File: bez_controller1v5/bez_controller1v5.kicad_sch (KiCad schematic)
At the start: 66 parts, among them J1 Conn_01x03_Male, J10 Screw_Terminal_01x02, J11 Conn_01x03_Male, J12 USB_B_Mini, J2 Conn_01x03_Male, J3 Conn_01x03_Male, J4 Conn_01x03_Male, J5 Conn_01x03_Male, J6 Conn_01x03_Male, J7 Conn_01x03_Male, J8 IMU Conn_01x08_Female, J9 JTAG Conn_01x06_Male, U1 74LVC2G241, U10 USBLC6-4SC6, U11 STM32F446RETx, U2 74LVC2G241, U3 74LVC2G241, U4 74LVC2G241, U5 74LVC2G241, U6 74LVC2G241, U7 PX07806-500-S, U8 LF50ABV_TO220, U9 LD1117AS33TR_SOT223, Y1 8MHz

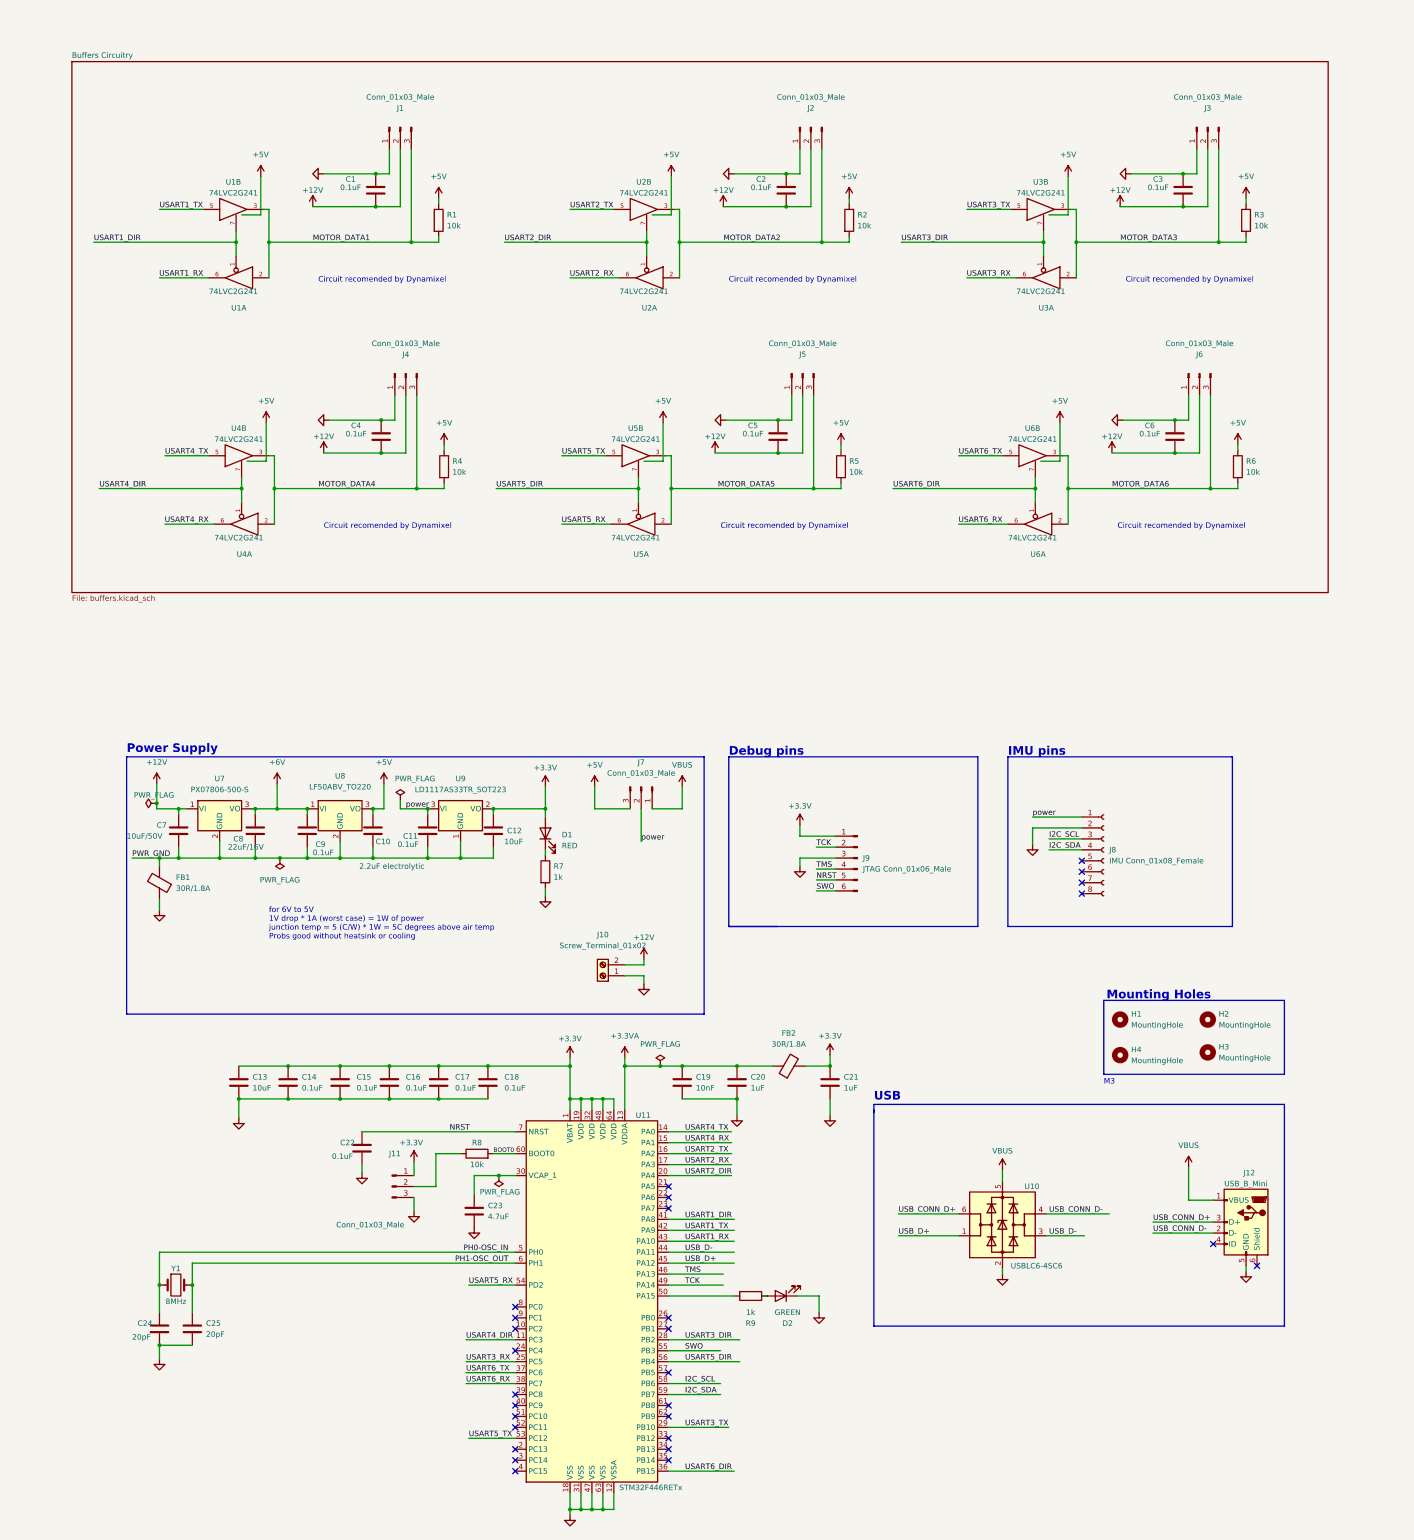
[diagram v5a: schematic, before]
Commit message: Added a means of measuring battery voltage and current + circuit protection
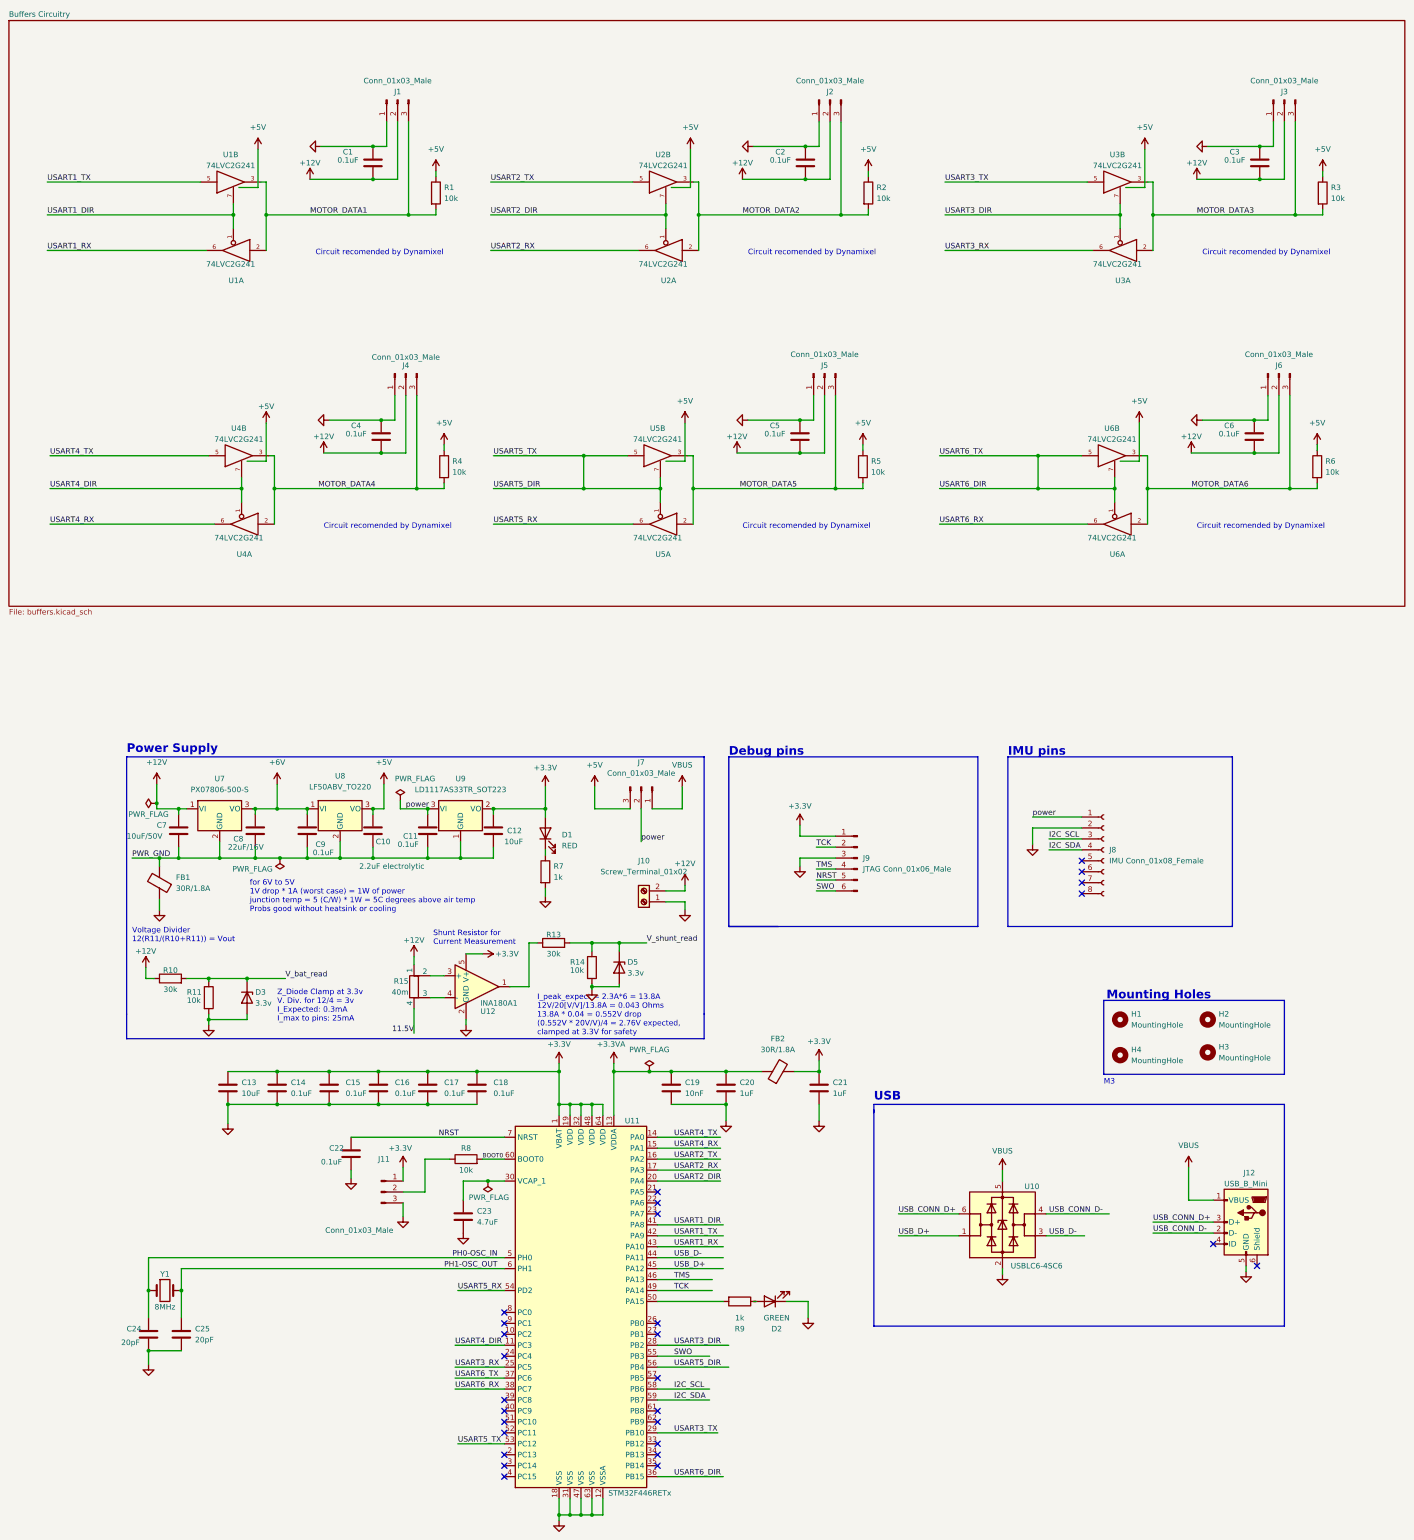
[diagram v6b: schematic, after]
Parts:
- added D3, D5: 3.3v, symbol Device:D_Zener
- added R10, R13: 30k, symbol Device:R
- added R11, R14: 10k, symbol Device:R
- added R15: 40m, symbol Device:R_Shunt
- added U12: INA180A1, Package_TO_SOT_SMD:SOT-23-5, symbol Amplifier_Current:INA180A1
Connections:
- net USART5_TX is gone; now on net USART5_DIR: U11.53 (PC12), U5.5
- net USART6_TX is gone; now on net USART6_DIR: U11.37 (PC6), U6.5
- net +12V: now also R10.1, R15.1
- net +3.3V: now also U12.5 (V+)
- net GND: now also D3.2 (A), D5.2 (A), R11.2, R14.2, U12.2 (GND)
- new net: R13.1, U12.1
- new net: R15.2, U12.3 (+)
- new net: R15.3, U12.4 (-)
- new net 11.5V: R15.4
- new net V_bat_read: D3.1 (K), R10.2, R11.1
- new net V_shunt_read: D5.1 (K), R13.2, R14.1
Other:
- note added: "I_peak_expect = 2.3A*6 = 13.8A 12V/20[V/V]/13.8A = 0.043 Ohms 13.8A * 0.04 = 0.552V drop (0.552V * 20V/V)/4 = 2.76V expected, clamped at 3.3V for safety"
- note added: "Shunt Resistor for Current Measurement"
- note added: "Voltage Divider 12(R11/(R10+R11)) = Vout"
- note added: "Z_Diode Clamp at 3.3v V. Div. for 12/4 = 3v I_Expected: 0.3mA I_max to pins: 25mA"
- moved on the sheet: C1, C13, C14, C15, C16, C17, C18, C19, C2, C20, C21, C22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

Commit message: new rounted PCB
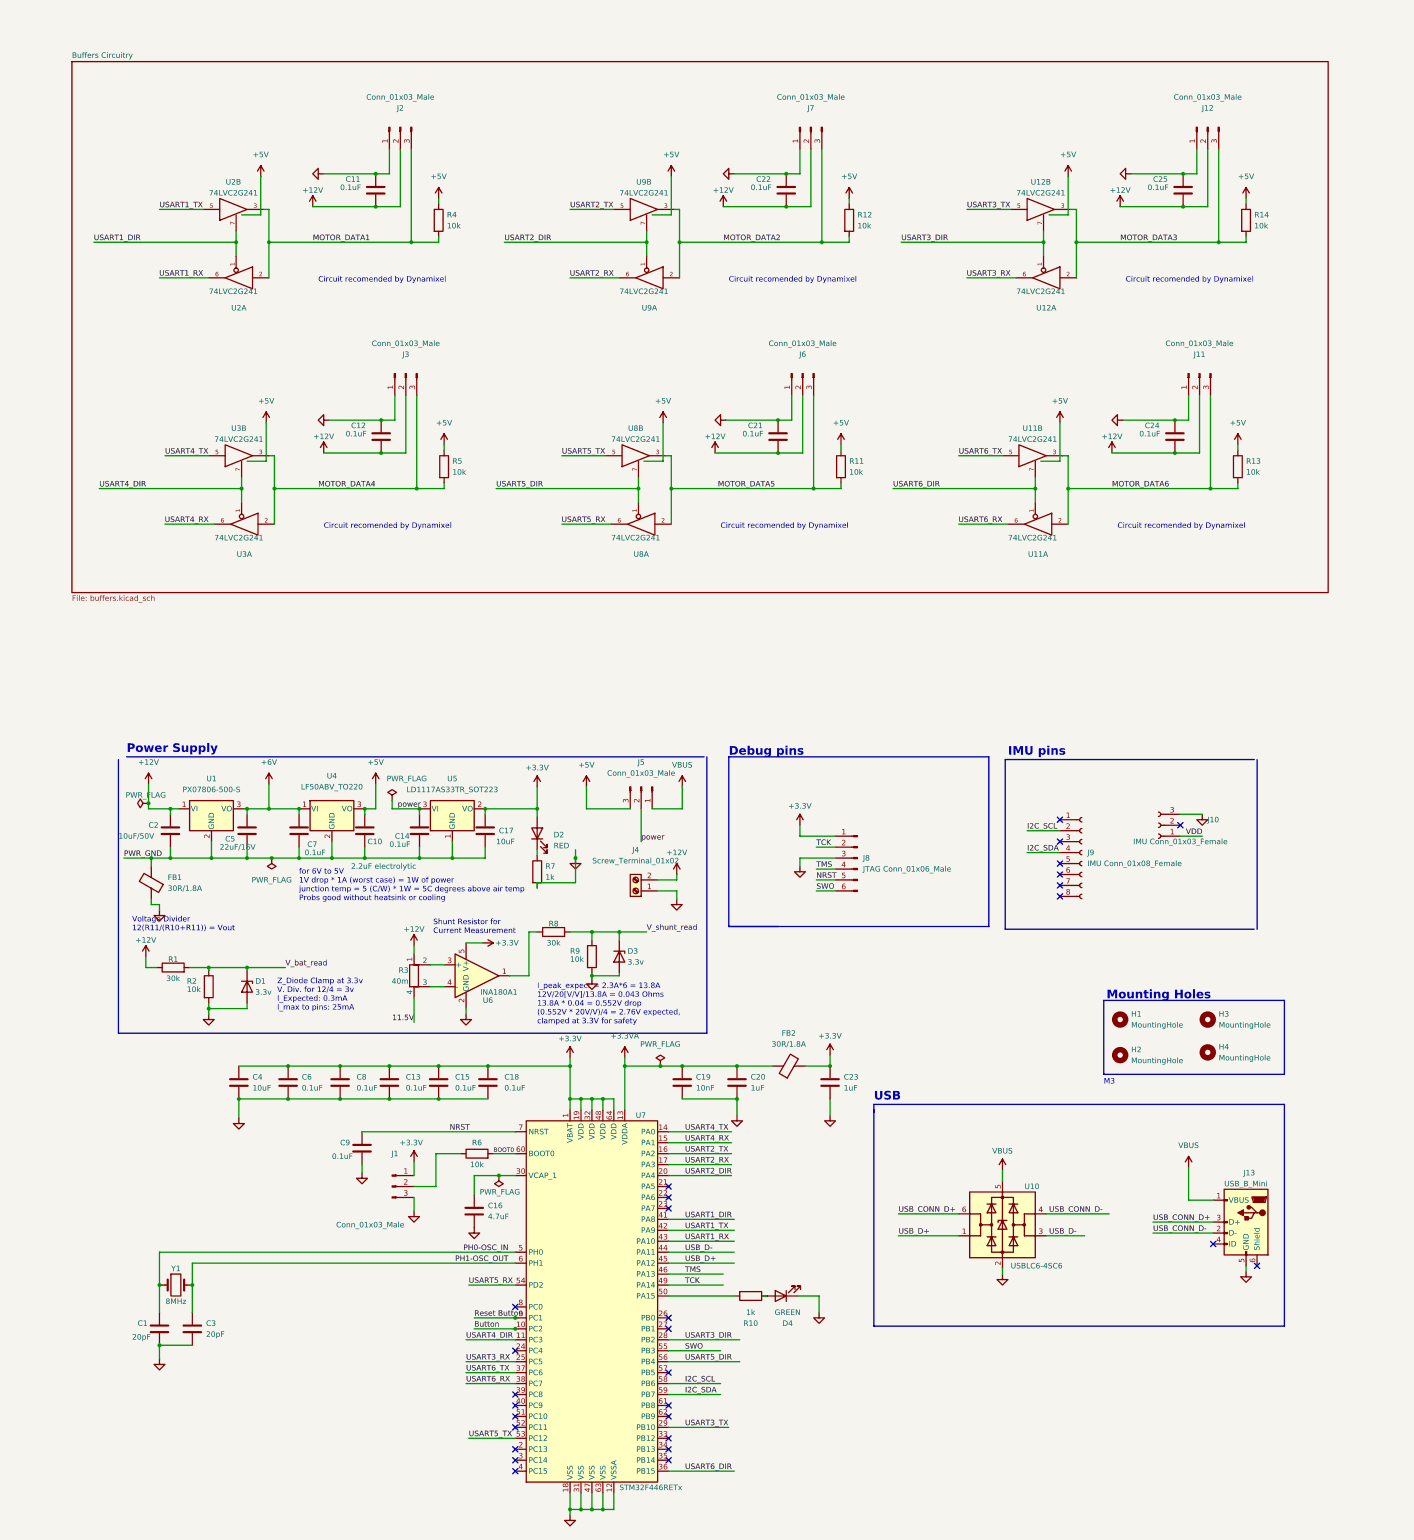
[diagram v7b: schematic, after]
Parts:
- removed D5: 3.3v, symbol Device:D_Zener
- removed R10, R13: 30k, symbol Device:R
- removed R11, R14: 10k, symbol Device:R
- removed R15: 40m, symbol Device:R_Shunt
- removed U12: INA180A1, Package_TO_SOT_SMD:SOT-23-5, symbol Amplifier_Current:INA180A1
- added D1: 3.3v, Diode_SMD:D_0603_1608Metric, symbol Device:D_Zener
- added J10: IMU Conn_01x03_Female, Connector_PinSocket_1.27mm:PinSocket_1x03_P1.27mm_Vertical, symbol Connector:Conn_01x08_Female
- added R1, R8: 30k, Resistor_SMD:R_0603_1608Metric, symbol Device:R
- added R2, R9: 10k, Resistor_SMD:R_0603_1608Metric, symbol Device:R
- added R3: 40m, Resistor_SMD:R_0603_1608Metric, symbol Device:R_Shunt
- added U6: INA180A1, Package_TO_SOT_SMD:SOT-23-5, symbol Amplifier_Current:INA180A1
- C1: renamed from C24; footprint Capacitor_THT:C_Disc_D5.0mm_W2.5mm_P5.00mm -> Capacitor_SMD:C_0603_1608Metric
- C10: footprint Capacitor_THT:C_Radial_D4.0mm_H7.0mm_P1.50mm -> Capacitor_SMD:CP_Elec_4x5.4
- C11: renamed from C1; footprint Capacitor_THT:C_Disc_D5.0mm_W2.5mm_P5.00mm -> Capacitor_SMD:C_0603_1608Metric
- C12: renamed from C4; footprint Capacitor_THT:C_Disc_D5.0mm_W2.5mm_P5.00mm -> Capacitor_SMD:C_0603_1608Metric
- C13: renamed from C16; footprint Capacitor_THT:C_Disc_D5.0mm_W2.5mm_P5.00mm -> Capacitor_SMD:C_0603_1608Metric
- C14: renamed from C11; footprint Capacitor_THT:C_Disc_D5.0mm_W2.5mm_P5.00mm -> Capacitor_SMD:C_0603_1608Metric
- C15: renamed from C17; footprint Capacitor_THT:C_Disc_D5.0mm_W2.5mm_P5.00mm -> Capacitor_SMD:C_0603_1608Metric
- C16: renamed from C23; footprint Capacitor_THT:C_Disc_D5.0mm_W2.5mm_P5.00mm -> Capacitor_SMD:C_0603_1608Metric
- C17: renamed from C12; footprint Capacitor_THT:C_Radial_D5.0mm_H11.0mm_P2.00mm -> Capacitor_SMD:C_0603_1608Metric
- C18, C19, C20: footprint Capacitor_THT:C_Disc_D5.0mm_W2.5mm_P5.00mm -> Capacitor_SMD:C_0603_1608Metric
- C2: renamed from C7; footprint Capacitor_THT:C_Radial_D5.0mm_H11.0mm_P2.00mm -> Capacitor_SMD:C_0805_2012Metric
- C21: renamed from C5; footprint Capacitor_THT:C_Disc_D5.0mm_W2.5mm_P5.00mm -> Capacitor_SMD:C_0603_1608Metric
- C22: renamed from C2; footprint Capacitor_THT:C_Disc_D5.0mm_W2.5mm_P5.00mm -> Capacitor_SMD:C_0603_1608Metric
- C23: renamed from C21; footprint Capacitor_THT:C_Disc_D5.0mm_W2.5mm_P5.00mm -> Capacitor_SMD:C_0603_1608Metric
- C24: renamed from C6; footprint Capacitor_THT:C_Disc_D5.0mm_W2.5mm_P5.00mm -> Capacitor_SMD:C_0603_1608Metric
- C25: renamed from C3; footprint Capacitor_THT:C_Disc_D5.0mm_W2.5mm_P5.00mm -> Capacitor_SMD:C_0603_1608Metric
- C3: renamed from C25; footprint Capacitor_THT:C_Disc_D5.0mm_W2.5mm_P5.00mm -> Capacitor_SMD:C_0603_1608Metric
- C4: renamed from C13; footprint Capacitor_THT:C_Radial_D5.0mm_H11.0mm_P2.00mm -> Capacitor_SMD:C_0603_1608Metric
- C5: renamed from C8; footprint Capacitor_THT:C_Radial_D5.0mm_H11.0mm_P2.00mm -> Capacitor_SMD:C_0805_2012Metric
- C6: renamed from C14; footprint Capacitor_THT:C_Disc_D5.0mm_W2.5mm_P5.00mm -> Capacitor_SMD:C_0603_1608Metric
- C7: renamed from C9; footprint Capacitor_THT:C_Disc_D5.0mm_W2.5mm_P5.00mm -> Capacitor_SMD:C_0603_1608Metric
- C8: renamed from C15; footprint Capacitor_THT:C_Disc_D5.0mm_W2.5mm_P5.00mm -> Capacitor_SMD:C_0603_1608Metric
- C9: renamed from C22; footprint Capacitor_THT:C_Disc_D5.0mm_W2.5mm_P5.00mm -> Capacitor_SMD:C_0603_1608Metric
- D3: footprint (none) -> Diode_SMD:D_0603_1608Metric
- J9: renamed from J8; footprint Connector_PinSocket_2.54mm:PinSocket_1x08_P2.54mm_Vertical -> Connector_PinSocket_1.27mm:PinSocket_1x08_P1.27mm_Vertical
- R10: renamed from R9; footprint Resistor_THT:R_Axial_DIN0204_L3.6mm_D1.6mm_P5.08mm_Horizontal -> Resistor_SMD:R_0603_1608Metric
- R11: renamed from R5; footprint Resistor_THT:R_Axial_DIN0204_L3.6mm_D1.6mm_P5.08mm_Horizontal -> Resistor_SMD:R_0603_1608Metric
- R12: renamed from R2; footprint Resistor_THT:R_Axial_DIN0204_L3.6mm_D1.6mm_P5.08mm_Horizontal -> Resistor_SMD:R_0603_1608Metric
- R13: renamed from R6; footprint Resistor_THT:R_Axial_DIN0204_L3.6mm_D1.6mm_P5.08mm_Horizontal -> Resistor_SMD:R_0603_1608Metric
- R14: renamed from R3; footprint Resistor_THT:R_Axial_DIN0204_L3.6mm_D1.6mm_P5.08mm_Horizontal -> Resistor_SMD:R_0603_1608Metric
- R4: renamed from R1; footprint Resistor_THT:R_Axial_DIN0204_L3.6mm_D1.6mm_P5.08mm_Horizontal -> Resistor_SMD:R_0603_1608Metric
- R5: renamed from R4; footprint Resistor_THT:R_Axial_DIN0204_L3.6mm_D1.6mm_P5.08mm_Horizontal -> Resistor_SMD:R_0603_1608Metric
- R6: renamed from R8; footprint Resistor_THT:R_Axial_DIN0204_L3.6mm_D1.6mm_P5.08mm_Horizontal -> Resistor_SMD:R_0603_1608Metric
- R7: footprint Resistor_THT:R_Axial_DIN0204_L3.6mm_D1.6mm_P5.08mm_Horizontal -> Resistor_SMD:R_0603_1608Metric
- renumbered D1 to D2, D2 to D4, H4 to H2, H2 to H3, H3 to H4, J11 to J1, J6 to J11, J3 to J12, J12 to J13, J1 to J2, J4 to J3, J10 to J4, J7 to J5, J5 to J6, J2 to J7, J9 to J8, U7 to U1, U6 to U11, U3 to U12, U1 to U2, U4 to U3, U8 to U4, U9 to U5, U11 to U7, U5 to U8, U2 to U9
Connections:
- net +12V: now also R1.1, R3.1
- net +3.3V: now also U6.5 (V+)
- net 11.5V: now also R3.4
- net GND: now also D1.2 (A), J10.3 (Pin_3), R2.2, R9.2, U6.2 (GND); no longer J9.2 (Pin_2)
- net I2C_SCL: now also J9.2 (Pin_2); no longer J9.3 (Pin_3)
- net USART5_DIR: no longer U7.53 (PC12), U8.5
- net USART6_DIR: no longer U11.5, U7.37 (PC6)
- net V_bat_read: now also D1.1 (K), R1.2, R2.1; no longer D3.1 (K)
- net V_shunt_read: now also D3.1 (K), R8.2, R9.1
- net power: no longer J9.1 (Pin_1)
- net Button: now reaches U7.10 (PC2)
- net Reset Button: now reaches U7.9 (PC1)
- new net: R3.2, U6.3 (+)
- new net: R3.3, U6.4 (-)
- new net: R8.1, U6.1
- new net USART5_TX: U7.53 (PC12), U8.5
- new net USART6_TX: U11.5, U7.37 (PC6)
- new net VDD: J10.1 (Pin_1)
- no-connect marks 28 -> 29
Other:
- moved on the sheet: C1, C10, C11, C13, C14, C15, C16, C17, C18, C19, C2, C20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
